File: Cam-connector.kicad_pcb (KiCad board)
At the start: 2 copper layers, 34.5 x 26.4 mm, 7 parts, among them J1 5051104096, J2 F304-1A7H1-11050-E100, U1 TSC2007IPW

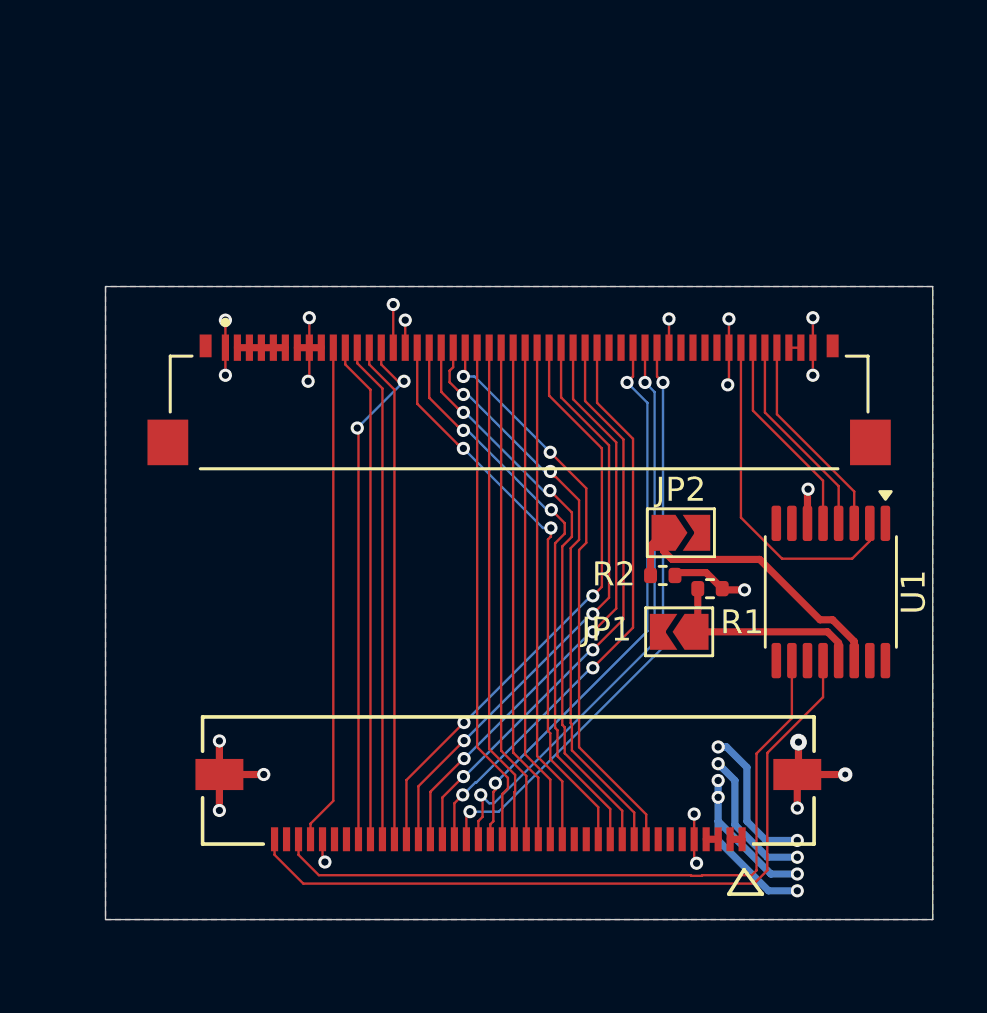
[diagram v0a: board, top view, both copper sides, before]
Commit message: Voltera printable board
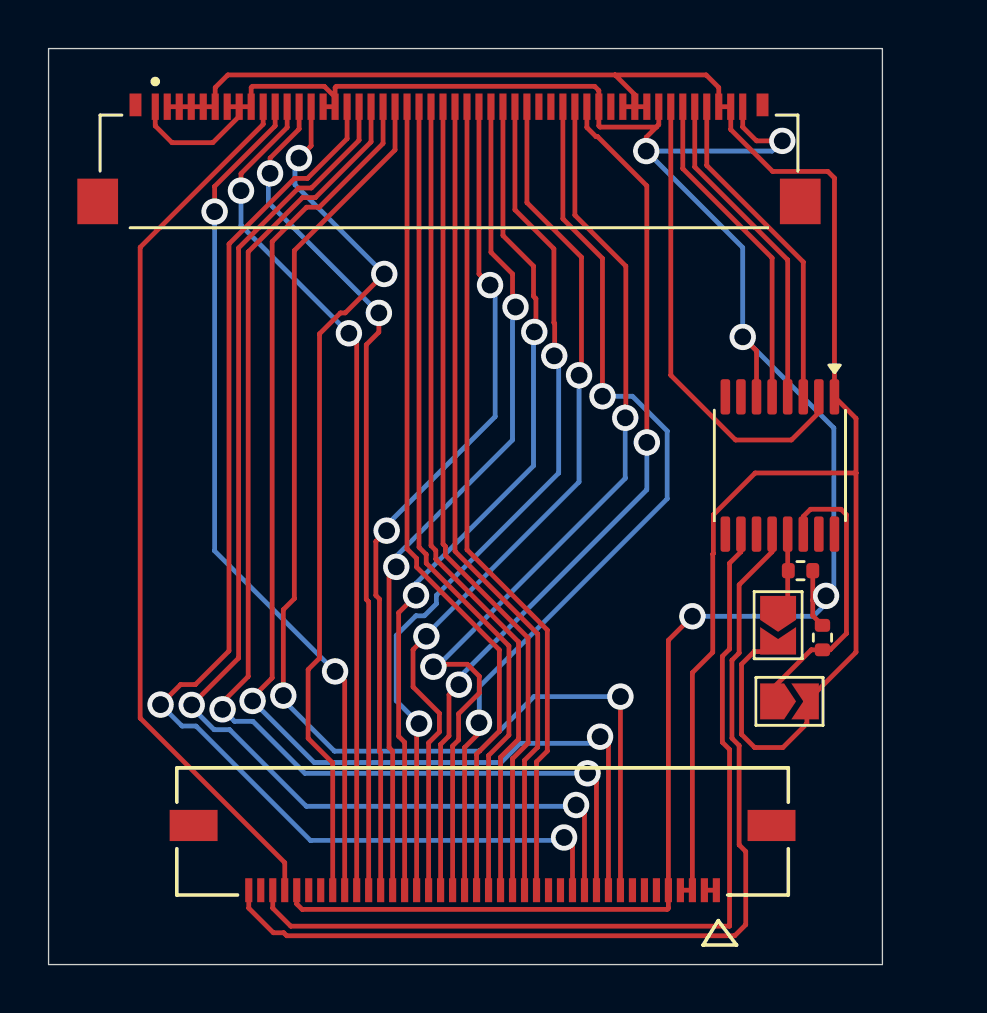
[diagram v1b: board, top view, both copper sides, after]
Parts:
- moved J2 10.5 mm to (156.7, 59.9)
- moved JP2 8.36 mm to (170.9, 82.0)
- moved R2 7.15 mm to (172.2, 79.3), turned to 90 degrees
- moved U1 5.69 mm to (170.5, 72.1)
- moved JP1 4.13 mm to (170.4, 78.8), turned to -90 degrees
- moved R1 3.85 mm to (171.3, 76.5)
- moved J1 2.38 mm to (158.1, 87.4)
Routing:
- net GND: track 32.6 -> 100.9 mm, vias 22 -> 5
- net SYS_3V3: track 26.1 -> 89.7 mm, vias 8 -> 0
- net /DB11: track 24.3 -> 50.6 mm
- net /DB15: track 24.1 -> 50.4 mm
- net /DB12: track 24.4 -> 49.9 mm
- net /DB14: track 24.3 -> 49.7 mm
- net /DB13: track 24.4 -> 49.4 mm
- net /LCD_RST: track 20.9 -> 37.3 mm
- net /LCD_B0: track 23.7 -> 38.7 mm
- net /LCD_VSYNC: track 20.9 -> 36.0 mm, vias 0 -> 2
- net /LCD_B1: track 24.6 -> 39.2 mm
- net /HSYNC: track 20.9 -> 35.5 mm, vias 0 -> 2
- net /DE: track 21.9 -> 36.4 mm
- net /DOTCLK: track 20.9 -> 35.4 mm, vias 0 -> 2
- net /DB9: track 21.0 -> 34.6 mm
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- removed copper zone on B.Cu, net GND
- removed copper zone on F.Cu, net SYS_3V3
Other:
- board size 34.5 x 26.4 mm -> 34.8 x 38.2 mm
